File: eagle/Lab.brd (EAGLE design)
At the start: 115 x 80 mm, 114 parts, among them IC1 FT232RL, IC2 74HC164D, IC3 ATMEGA328AU/TQFP, IC4 74FST3257, IC5 74FST3257, P1 TSM-108-02-L-SV, P2 TSM-106-02-L-SV, P3 TSM-110-02-L-SV, P4 TSM-108-02-L-SV, Q1 LFXTAL003237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

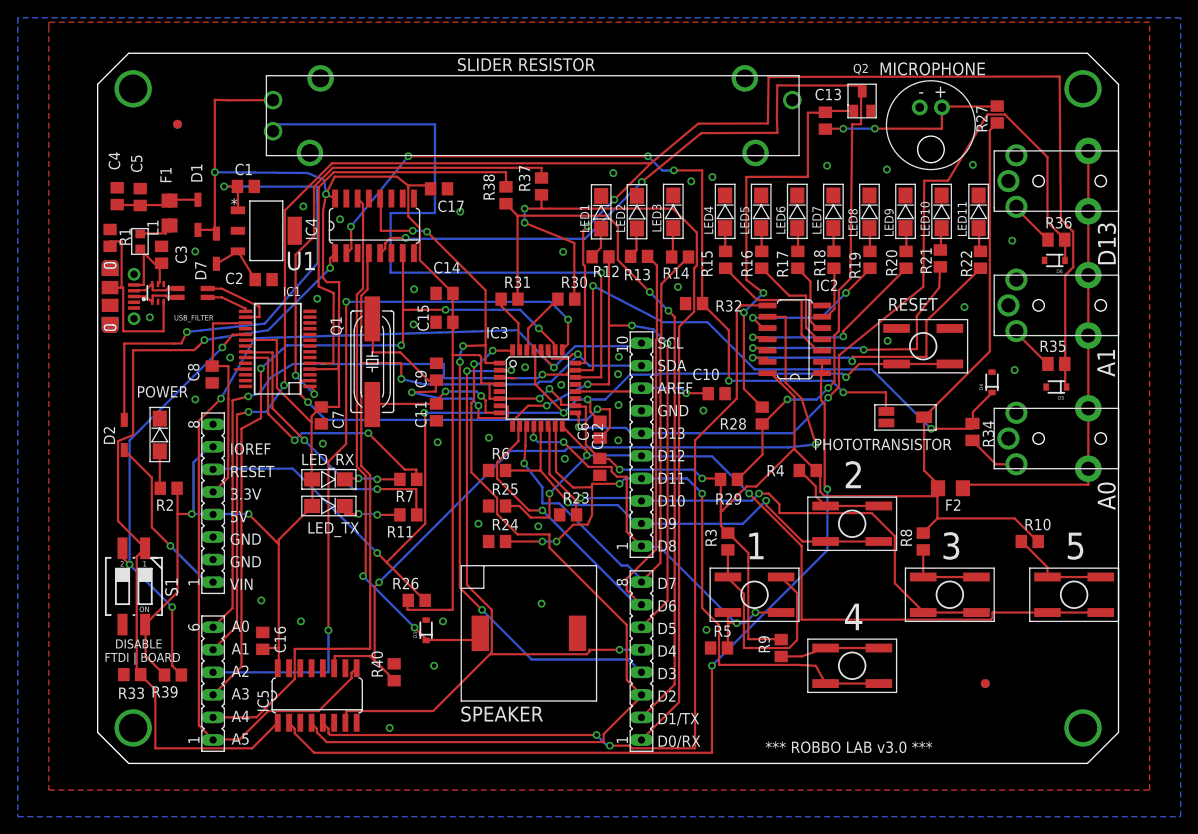
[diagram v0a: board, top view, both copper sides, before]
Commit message: Add 3d models. Changed gerbers for manufacturing on Rezonit
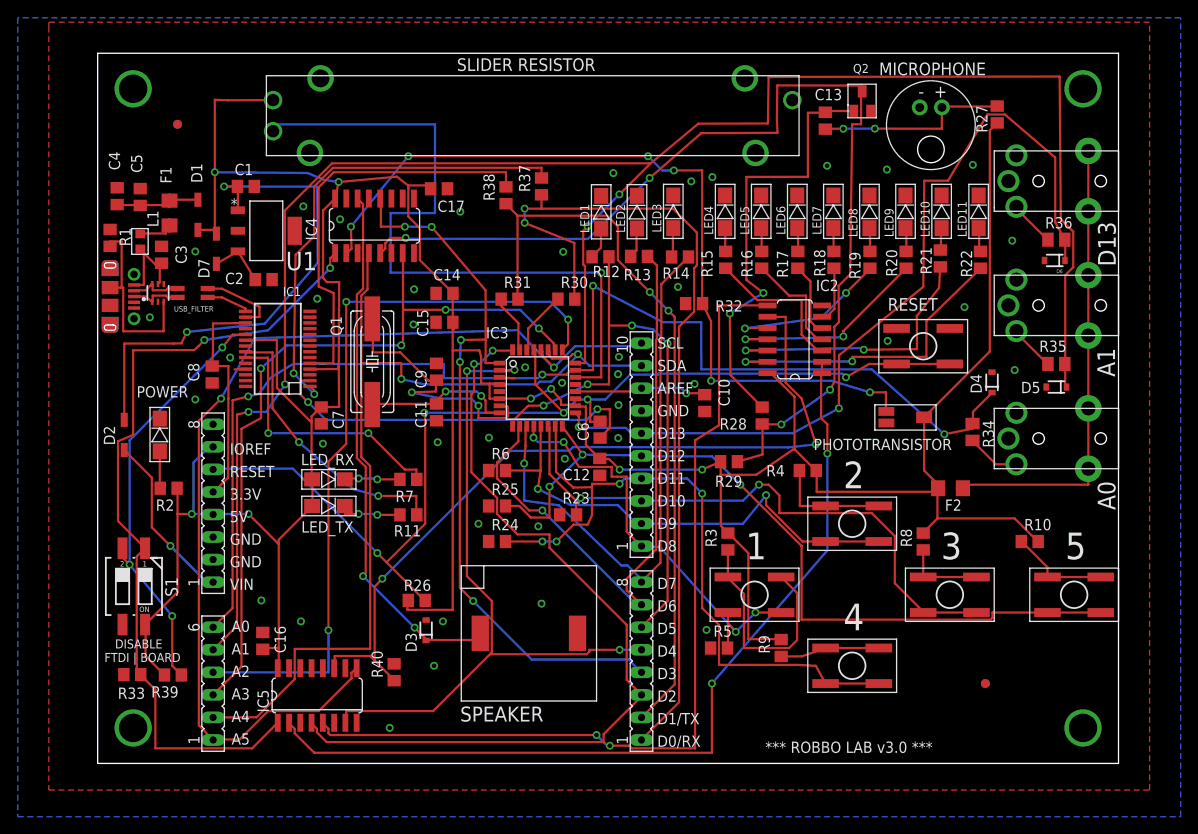
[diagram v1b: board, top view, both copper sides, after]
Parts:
- added DRILEGEND: (no value), drilegend:DRILEGEND
- moved R29 2.00 mm to (71.1, 34.0)
- moved C10 1.71 mm to (68.4, 40.6), turned to 90 degrees
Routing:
- net PC0: track 133.8 -> 137.0 mm
- net PB0: track 47.4 -> 49.6 mm
- net PB1: track 53.0 -> 55.1 mm
- net CLK: track 98.5 -> 100.3 mm
- net N$78: track 48.1 -> 49.9 mm
- net N$37: track 11.3 -> 13.0 mm
- net +5V: track 405.3 -> 403.7 mm
- net N$57: track 22.7 -> 24.2 mm
- net N$58: track 30.7 -> 32.1 mm
- net PB2: track 66.4 -> 67.8 mm
- net N$56: track 17.7 -> 19.1 mm
- net MIC: track 118.1 -> 116.9 mm
- net N$59: track 34.9 -> 36.0 mm
- net PB5: track 93.9 -> 94.9 mm
- net PD3: track 82.2 -> 83.2 mm
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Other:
- outline, holes or cut-outs redrawn
- board text added: "01-16"
- board text added: "01-20"
- board text added: "LAYER-STACK"
